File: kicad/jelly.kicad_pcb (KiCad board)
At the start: 2 copper layers, 59.9 x 32.9 mm, 41 parts, among them M1 PAGER_MOTOR, M2 PAGER_MOTOR, P1 CONN_01X01, P10 CONN_01X01, P11 CONN_01X01, P12 CONN_01X01, P13 CONN_01X01, P14 CONN_01X01, P15 CONN_01X01, P2 CONN_01X01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

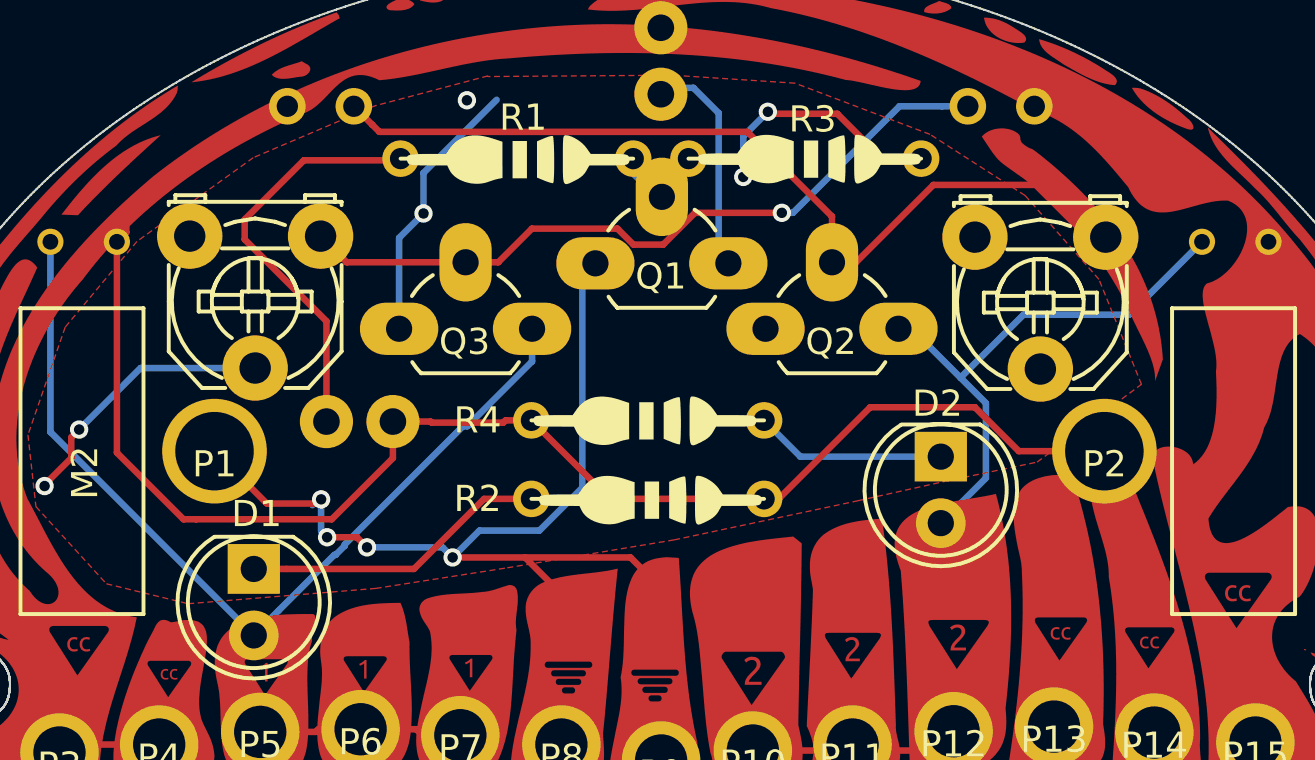
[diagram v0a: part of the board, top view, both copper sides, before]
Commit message: Fix some traces
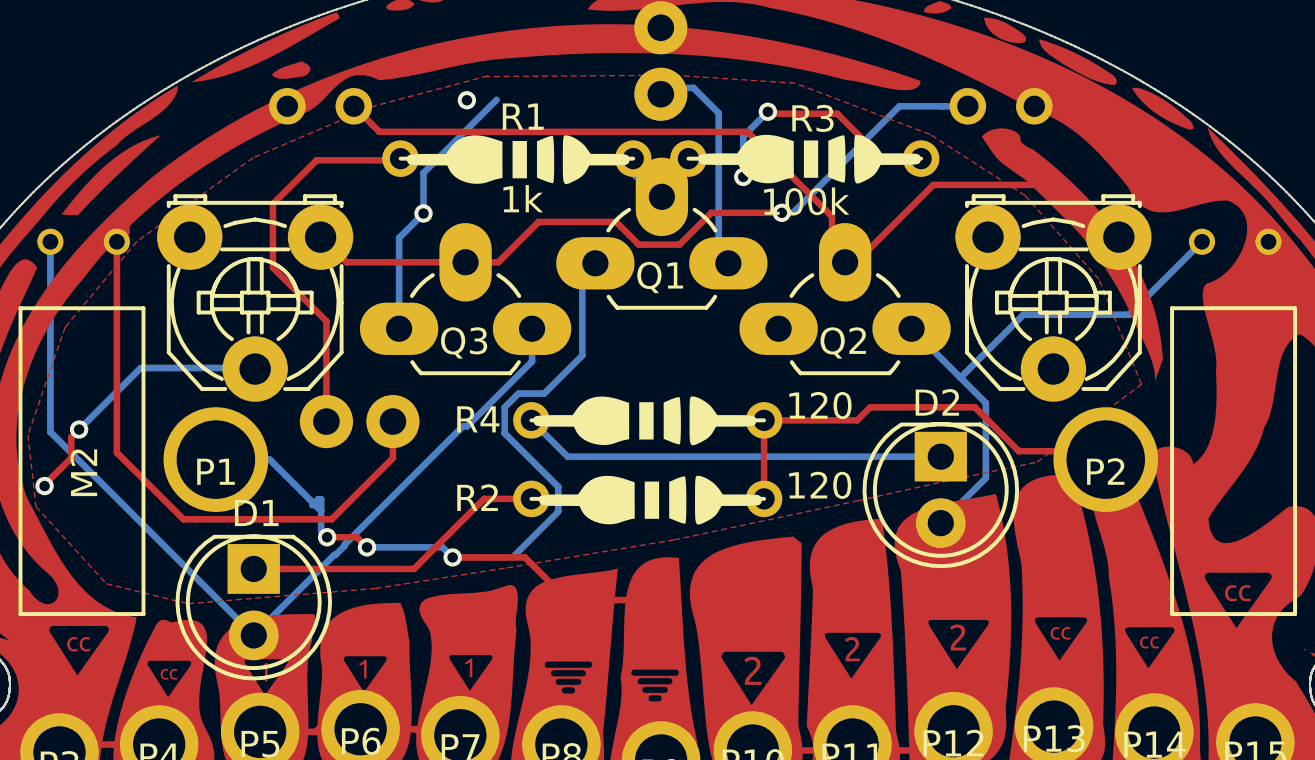
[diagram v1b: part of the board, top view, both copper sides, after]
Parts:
- moved Q2 0.50 mm to (154.6, 78.3)
- moved RV2 0.50 mm to (167.6, 74.8)
- moved P1 0.33 mm to (133.1, 83.3)
- moved P2 0.33 mm to (167.1, 83.3)
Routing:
- net VCC: track 65.5 -> 55.6 mm
- net Net-(D2-Pad1): track 10.6 -> 16.2 mm
- net Net-(R1-Pad1): track 15.5 -> 14.3 mm
- net GND: track 69.3 -> 69.7 mm, vias 9 -> 8

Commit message: Rename leds from D to LED
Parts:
- BT1, SW1: footprint custom:Pin_Header_Straight_1x02 -> KiCad/Pin_Headers.pretty:Pin_Header_Straight_1x02
- renumbered D1 to LED1, D2 to LED2

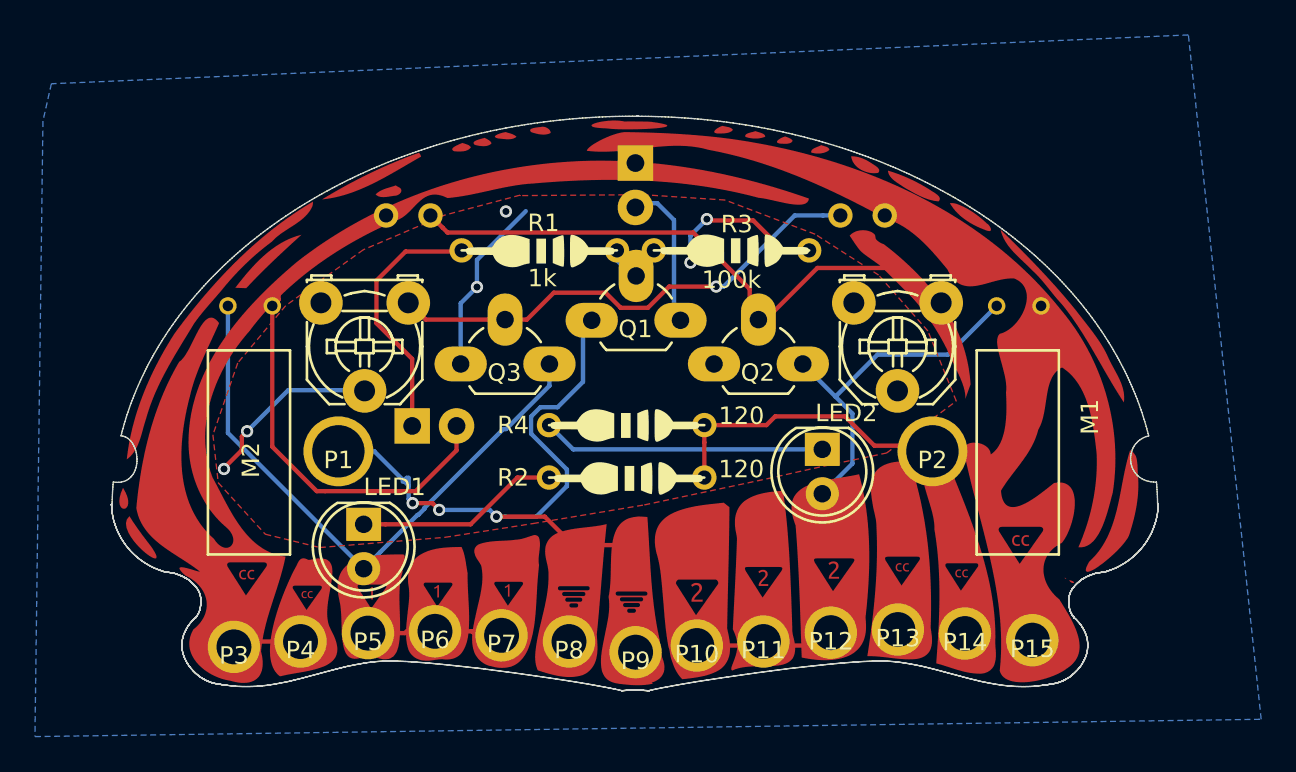
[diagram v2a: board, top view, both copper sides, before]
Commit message: Add page motor silkscreen image
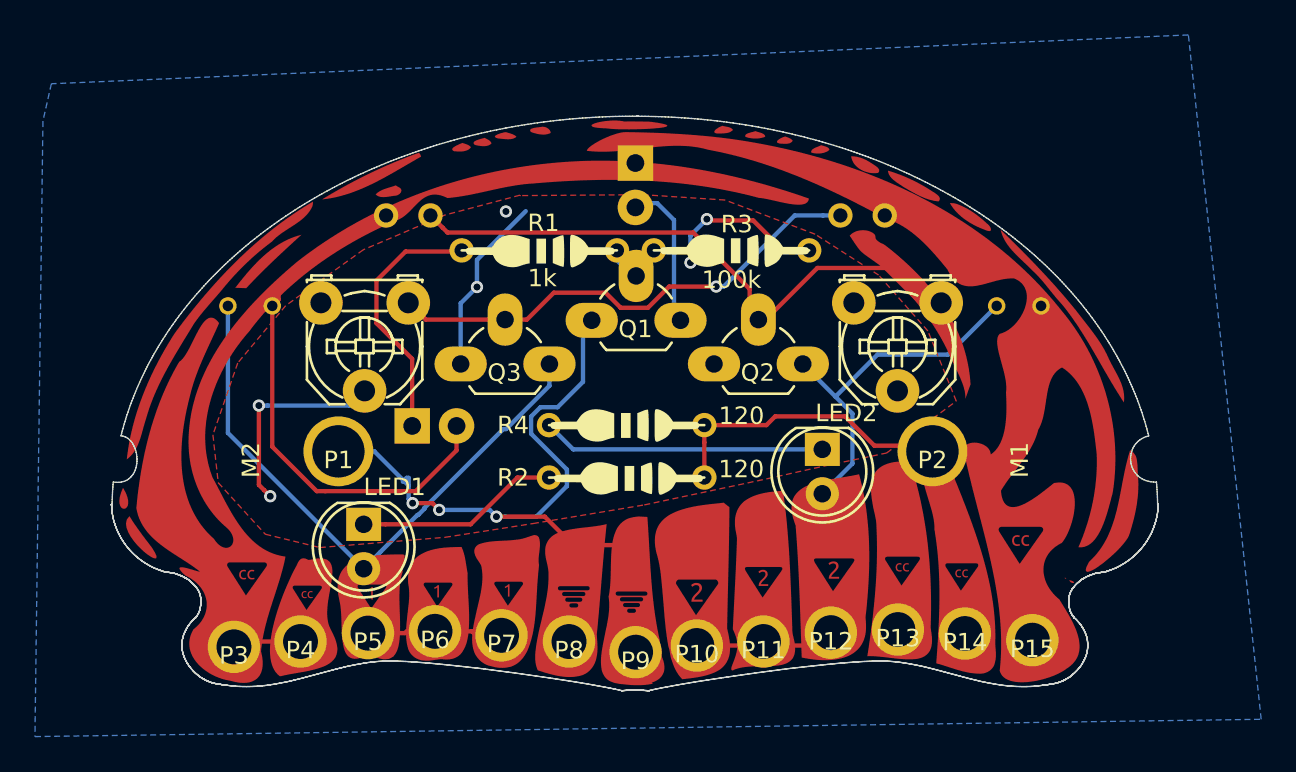
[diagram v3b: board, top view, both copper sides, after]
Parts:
- added DNP10: pager_motor_image1, custom:page_motor_image, B.Cu at (173.3, 81.8)
- added DNP11: pager_motor_image2, custom:page_motor_image_flipped, F.Cu at (126.7, 81.9)
- moved DNP4 9.65 mm to (165.0, 86.6)
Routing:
- net GND: track 69.7 -> 71.1 mm

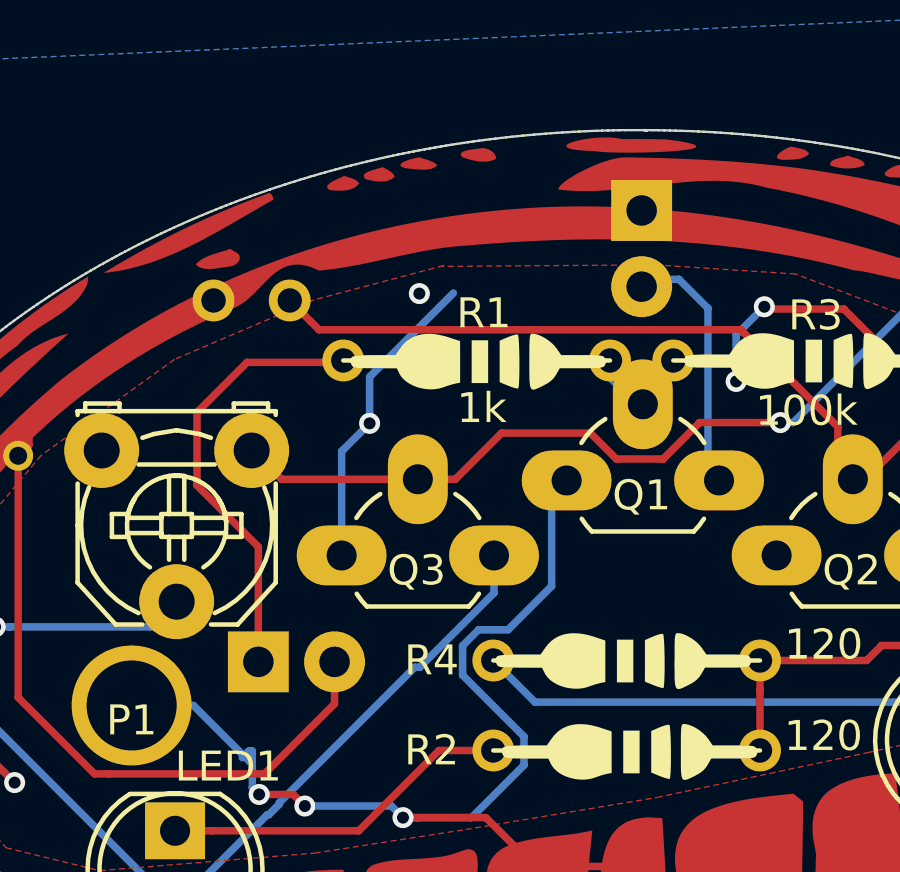
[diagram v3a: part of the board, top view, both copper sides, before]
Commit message: Adjust LDR silkscreen brackets
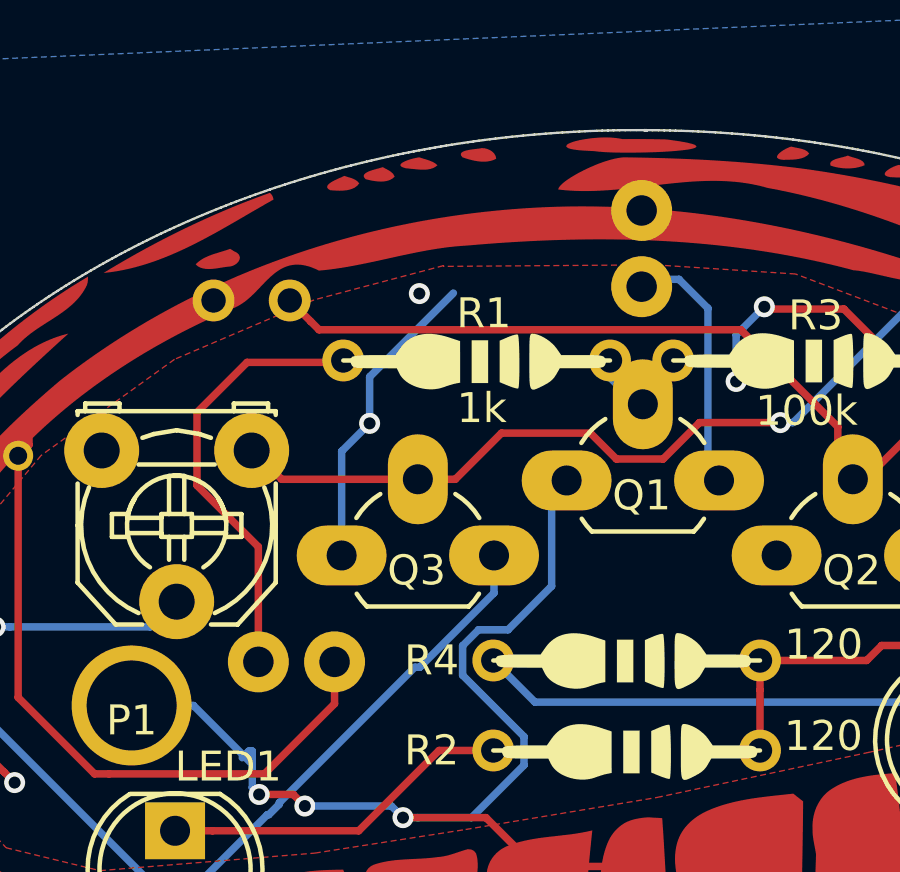
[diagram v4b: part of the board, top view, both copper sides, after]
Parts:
- BT1, SW1: footprint KiCad/Pin_Headers.pretty:Pin_Header_Straight_1x02 -> custom:Pin_Header_Straight_1x02
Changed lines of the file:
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@@
     (add_net Vout2)
+  )
+  (module custom:Pin_Header_Straight_1x02 (layer B.Cu)
+    (at 150.053 66.823 180)
+    (descr "Through hole pin header")
+    (tags "pin header")
+    (fp_text reference BT1 (at 0 5.1 180) (layer B.SilkS)
+      (effects (font (size 1 1) (thickness 0.15)) (justify mirror))
+    )
+    (fp_text value BATTERY (at 0 4 180) (layer B.Fab)
+      (effects (font (size 1 1) (thickness 0.15)) (justify mirror))
+    )
+    (fp_line (start -1.75 -4.3) (end 1.75 -4.3) (layer B.CrtYd) (width 0.05))
+    (fp_line (start -1.75 1.75) (end 1.75 1.75) (layer B.CrtYd) (width 0.05))
+    (fp_line (start 1.75 1.75) (end 1.75 -4.3) (layer B.CrtYd) (width 0.05))
+    (fp_line (start -1.75 1.75) (end -1.75 -4.3) (layer B.CrtYd) (width 0.05))
+    (pad 2 thru_hole oval (at 0 -2.54 180) (size 2.032 2.032) (drill 1.016) (layers *.Cu *.Mask B.SilkS)
+      (net 8 "Net-(BT1-Pad2)"))
+    (pad 1 thru_hole circle (at 0 0 180) (size 2.032 2.032) (drill 1.016) (layers *.Cu *.Mask B.SilkS)
+      (net 1 VCC))
+    (model Pin_Headers.3dshapes/Pin_Header_Straight_1x02.wrl
+      (at (xyz 0 -0.05 0))
+      (scale (xyz 1 1 1))
+      (rotate (xyz 0 0 90))
+    )
+  )
+  (module custom:Pin_Header_Straight_1x02 (layer B.Cu)
+    (at 137.2768 81.869 270)
+    (descr "Through hole pin header")
+    (tags "pin header")
+    (fp_text reference SW1 (at 0 5.1 270) (layer B.SilkS)
+      (effects (font (size 1 1) (thickness 0.15)) (justify mirror))
+    )
+    (fp_text value SPST (at 0 4 270) (layer B.Fab)
+      (effects (font (size 1 1) (thickness 0.15)) (justify mirror))
+    )
+    (fp_line (start -1.75 -4.3) (end 1.75 -4.3) (layer B.CrtYd) (width 0.05))
+    (fp_line (start -1.75 1.75) (end 1.75 1.75) (layer B.CrtYd) (width 0.05))
+    (fp_line (start 1.75 1.75) (end 1.75 -4.3) (layer B.CrtYd) (width 0.05))
+    (fp_line (start -1.75 1.75) (end -1.75 -4.3) (layer B.CrtYd) (width 0.05))
+    (pad 2 thru_hole oval (at 0 -2.54 270) (size 2.032 2.032) (drill 1.016) (layers *.Cu *.Mask B.SilkS)
+      (net 1 VCC))
+    (pad 1 thru_hole circle (at 0 0 270) (size 2.032 2.032) (drill 1.016) (layers *.Cu *.Mask B.SilkS)
+      (net 11 "Net-(R1-Pad1)"))
+    (model Pin_Headers.3dshapes/Pin_Header_Straight_1x02.wrl
+      (at (xyz 0 -0.05 0))
+      (scale (xyz 1 1 1))
+      (rotate (xyz 0 0 90))
+    )
+  )
+  (module custom:ldr (layer F.Cu)
+    (at 137.053 69.823 180)
+    (descr "Resistance verticale")
+    (tags R)
+    (fp_text reference PHOTO2 (at 2.81 2.87 180) (layer F.SilkS) hide
+      (effects (font (size 1 1) (thickness 0.15)))
+    )
+    (fp_text value Photores (at -0.05 -1.78 180) (layer F.Fab) hide
+      (effects (font (size 1 1) (thickness 0.15)))
+    )
+    (fp_arc (start 1.02 -0.04) (end 2.29 -1.31) (angle 90) (layer B.SilkS) (width 0.15))
+    (fp_arc (start -0.87 -0.02) (end -2.14 1.25) (angle 90) (layer B.SilkS) (width 0.15))
+    (pad 2 thru_hole circle (at 1.27 0 180) (size 1.397 1.397) (drill 0.8128) (layers *.Cu *.Mask)
+      (net 1 VCC))
+    (pad 1 thru_hole circle (at -1.27 0 180) (size 1.397 1.397) (drill 0.8128) (layers *.Cu *.Mask)
+      (net 6 "Net-(PHOTO2-Pad1)"))
+  )
+  (module custom:ldr (layer F.Cu)
+    (at 163.053 69.823)
+    (descr "Resistance verticale")
+    (tags R)
+    (fp_text reference PHOTO1 (at 2.81 2.87) (layer F.SilkS) hide
+      (effects (font (size 1 1) (thickness 0.15)))
+    )
+    (fp_text value Photores (at -0.05 -1.78) (layer F.Fab) hide
+      (effects (font (size 1 1) (thickness 0.15)))
+    )
+    (fp_arc (start 1.02 -0.04) (end 2.29 -1.31) (angle 90) (layer B.SilkS) (width 0.15))
+    (fp_arc (start -0.87 -0.02) (end -2.14 1.25) (angle 90) (layer B.SilkS) (width 0.15))
+    (pad 2 thru_hole circle (at 1.27 0) (size 1.397 1.397) (drill 0.8128) (layers *.Cu *.Mask)
+      (net 1 VCC))
+    (pad 1 thru_hole circle (at -1.27 0) (size 1.397 1.397) (drill 0.8128) (layers *.Cu *.Mask)
+      (net 7 "Net-(PHOTO1-Pad1)"))
   )
   (module custom:page_motor_image_flipped (layer F.Cu)
@@
       (net 1 VCC))
   )
-  (module KiCad/Pin_Headers.pretty:Pin_Header_Straight_1x02 (layer B.Cu)
-    (at 150.053 66.823 180)
-    (descr "Through hole pin header")
-    (tags "pin header")
-    (fp_text reference BT1 (at 0 5.1 180) (layer B.SilkS)
-      (effects (font (size 1 1) (thickness 0.15)) (justify mirror))
-    )
-    (fp_text value BATTERY (at 0 3.1 180) (layer B.Fab)
-      (effects (font (size 1 1) (thickness 0.15)) (justify mirror))
-    )
-    (fp_line (start -1.27 -3.81) (end 1.27 -3.81) (layer B.SilkS) (width 0.15))
-    (fp_line (start -1.27 -1.27) (end -1.27 -3.81) (layer B.SilkS) (width 0.15))
-    (fp_line (start -1.55 1.55) (end 1.55 1.55) (layer B.SilkS) (width 0.15))
-    (fp_line (start -1.55 0) (end -1.55 1.55) (layer B.SilkS) (width 0.15))
-    (fp_line (start 1.27 -1.27) (end -1.27 -1.27) (layer B.SilkS) (width 0.15))
-    (fp_line (start -1.75 -4.3) (end 1.75 -4.3) (layer B.CrtYd) (width 0.05))
-    (fp_line (start -1.75 1.75) (end 1.75 1.75) (layer B.CrtYd) (width 0.05))
-    (fp_line (start 1.75 1.75) (end 1.75 -4.3) (layer B.CrtYd) (width 0.05))
-    (fp_line (start -1.75 1.75) (end -1.75 -4.3) (layer B.CrtYd) (width 0.05))
-    (fp_line (start 1.55 1.55) (end 1.55 0) (layer B.SilkS) (width 0.15))
-    (fp_line (start 1.27 -1.27) (end 1.27 -3.81) (layer B.SilkS) (width 0.15))
-    (pad 2 thru_hole oval (at 0 -2.54 180) (size 2.032 2.032) (drill 1.016) (layers *.Cu *.Mask B.SilkS)
-      (net 8 "Net-(BT1-Pad2)"))
-    (pad 1 thru_hole rect (at 0 0 180) (size 2.032 2.032) (drill 1.016) (layers *.Cu *.Mask B.SilkS)
-      (net 1 VCC))
-    (model Pin_Headers.3dshapes/Pin_Header_Straight_1x02.wrl
-      (at (xyz 0 -0.05 0))
-      (scale (xyz 1 1 1))
-      (rotate (xyz 0 0 90))
-    )
-  )
-  (module KiCad/Pin_Headers.pretty:Pin_Header_Straight_1x02 (layer B.Cu)
-    (at 137.2768 81.869 270)
-    (descr "Through hole pin header")
-    (tags "pin header")
-    (fp_text reference SW1 (at 0 5.1 270) (layer B.SilkS)
-      (effects (font (size 1 1) (thickness 0.15)) (justify mirror))
-    )
-    (fp_text value SPST (at 0 3.1 270) (layer B.Fab)
-      (effects (font (size 1 1) (thickness 0.15)) (justify mirror))
-    )
-    (fp_line (start 1.27 -1.27) (end 1.27 -3.81) (layer B.SilkS) (width 0.15))
-    (fp_line (start 1.55 1.55) (end 1.55 0) (layer B.SilkS) (width 0.15))
-    (fp_line (start -1.75 1.75) (end -1.75 -4.3) (layer B.CrtYd) (width 0.05))
-    (fp_line (start 1.75 1.75) (end 1.75 -4.3) (layer B.CrtYd) (width 0.05))
-    (fp_line (start -1.75 1.75) (end 1.75 1.75) (layer B.CrtYd) (width 0.05))
-    (fp_line (start -1.75 -4.3) (end 1.75 -4.3) (layer B.CrtYd) (width 0.05))
-    (fp_line (start 1.27 -1.27) (end -1.27 -1.27) (layer B.SilkS) (width 0.15))
-    (fp_line (start -1.55 0) (end -1.55 1.55) (layer B.SilkS) (width 0.15))
-    (fp_line (start -1.55 1.55) (end 1.55 1.55) (layer B.SilkS) (width 0.15))
-    (fp_line (start -1.27 -1.27) (end -1.27 -3.81) (layer B.SilkS) (width 0.15))
-    (fp_line (start -1.27 -3.81) (end 1.27 -3.81) (layer B.SilkS) (width 0.15))
-    (pad 1 thru_hole rect (at 0 0 270) (size 2.032 2.032) (drill 1.016) (layers *.Cu *.Mask B.SilkS)
-      (net 11 "Net-(R1-Pad1)"))
-    (pad 2 thru_hole oval (at 0 -2.54 270) (size 2.032 2.032) (drill 1.016) (layers *.Cu *.Mask B.SilkS)
-      (net 1 VCC))
-    (model Pin_Headers.3dshapes/Pin_Header_Straight_1x02.wrl
-      (at (xyz 0 -0.05 0))
-      (scale (xyz 1 1 1))
-      (rotate (xyz 0 0 90))
-    )
-  )
   (module custom:resistor (layer F.Cu)
     (at 144.593 71.873)
@@
       (xy -4.199589 -0.16433)) (layer F.SilkS) (width 0))
   )
-  (module custom:ldr (layer F.Cu)
-    (at 137.053 69.823 180)
-    (descr "Resistance verticale")
-    (tags R)
-    (fp_text reference PHOTO2 (at 2.81 2.87 180) (layer F.SilkS) hide
-      (effects (font (size 1 1) (thickness 0.15)))
-    )
-    (fp_text value Photores (at -0.05 -1.78 180) (layer F.Fab) hide
-      (effects (font (size 1 1) (thickness 0.15)))
-    )
-    (fp_arc (start 1.27 0) (end 2.54 -1.27) (angle 90) (layer B.SilkS) (width 0.15))
-    (fp_arc (start -1.27 0) (end -2.54 1.27) (angle 90) (layer B.SilkS) (width 0.15))
-    (pad 1 thru_hole circle (at -1.27 0 180) (size 1.397 1.397) (drill 0.8128) (layers *.Cu *.Mask)
-      (net 6 "Net-(PHOTO2-Pad1)"))
-    (pad 2 thru_hole circle (at 1.27 0 180) (size 1.397 1.397) (drill 0.8128) (layers *.Cu *.Mask)
-      (net 1 VCC))
-  )
   (module custom:R3-5 (layer F.Cu)
     (at 144.553 71.823)
@@
     )
   )
-  (module custom:ldr (layer F.Cu)
-    (at 163.053 69.823)
-    (descr "Resistance verticale")
-    (tags R)
-    (fp_text reference PHOTO1 (at 2.81 2.87) (layer F.SilkS) hide
-      (effects (font (size 1 1) (thickness 0.15)))
-    )
-    (fp_text value Photores (at -0.05 -1.78) (layer F.Fab) hide
-      (effects (font (size 1 1) (thickness 0.15)))
-    )
-    (fp_arc (start -1.27 0) (end -2.54 1.27) (angle 90) (layer B.SilkS) (width 0.15))
-    (fp_arc (start 1.27 0) (end 2.54 -1.27) (angle 90) (layer B.SilkS) (width 0.15))
-    (pad 1 thru_hole circle (at -1.27 0) (size 1.397 1.397) (drill 0.8128) (layers *.Cu *.Mask)
-      (net 7 "Net-(PHOTO1-Pad1)"))
-    (pad 2 thru_hole circle (at 1.27 0) (size 1.397 1.397) (drill 0.8128) (layers *.Cu *.Mask)
-      (net 1 VCC))
-  )
   (module custom:ldr_image_flipped (layer F.Cu)

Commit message: Add plus and minus labels
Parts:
- added DNP12: plus1, custom:plus, B.Cu at (147.7, 66.8)
- added DNP13: minus1, custom:minus, B.Cu at (152.4, 69.4)
- moved DNP2 0.66 mm to (157.2, 68.4)
- moved DNP3 0.51 mm to (143.1, 68.5)
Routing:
- net GND: track 71.1 -> 74.8 mm, vias 8 -> 9
- net (no net): vias 1 -> 0
